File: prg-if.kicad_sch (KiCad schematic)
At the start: 30 parts

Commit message: Add power supply.
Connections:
- net P_5V_USB renamed PRG_USB_5V
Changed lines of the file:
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@@
     (effects (font (size 1.27 1.27)) (justify left))
   )
-  (hierarchical_label "P_5V_USB" (shape output) (at 46.99 92.71 0)
+  (hierarchical_label "PRG_USB_5V" (shape output) (at 46.99 92.71 0)
     (effects (font (size 1.27 1.27)) (justify left))
   )
@@
   )
   (symbol (lib_id "Interface_USB:FT2232HL") (at 129.54 114.3 0) (unit 1)
-    (in_bom yes) (on_board yes) (fields_autoplaced)
-    (property "Reference" "U?" (id 0) (at 144.2594 58.5302 0)
-      (effects (font (size 1.27 1.27)) (justify left))
-    )
-    (property "Value" "FT2232HL" (id 1) (at 144.2594 61.0671 0)
-      (effects (font (size 1.27 1.27)) (justify left))
-    )
+    (in_bom yes) (on_board yes)
+    (property "Reference" "U?" (id 0) (at 129.54 113.0331 0))
+    (property "Value" "FT2232HL" (id 1) (at 129.54 115.57 0))
     (property "Footprint" "Package_QFP:LQFP-64_10x10mm_P0.5mm" (id 2) (at 129.54 114.3 0)
       (effects (font (size 1.27 1.27)) hide)

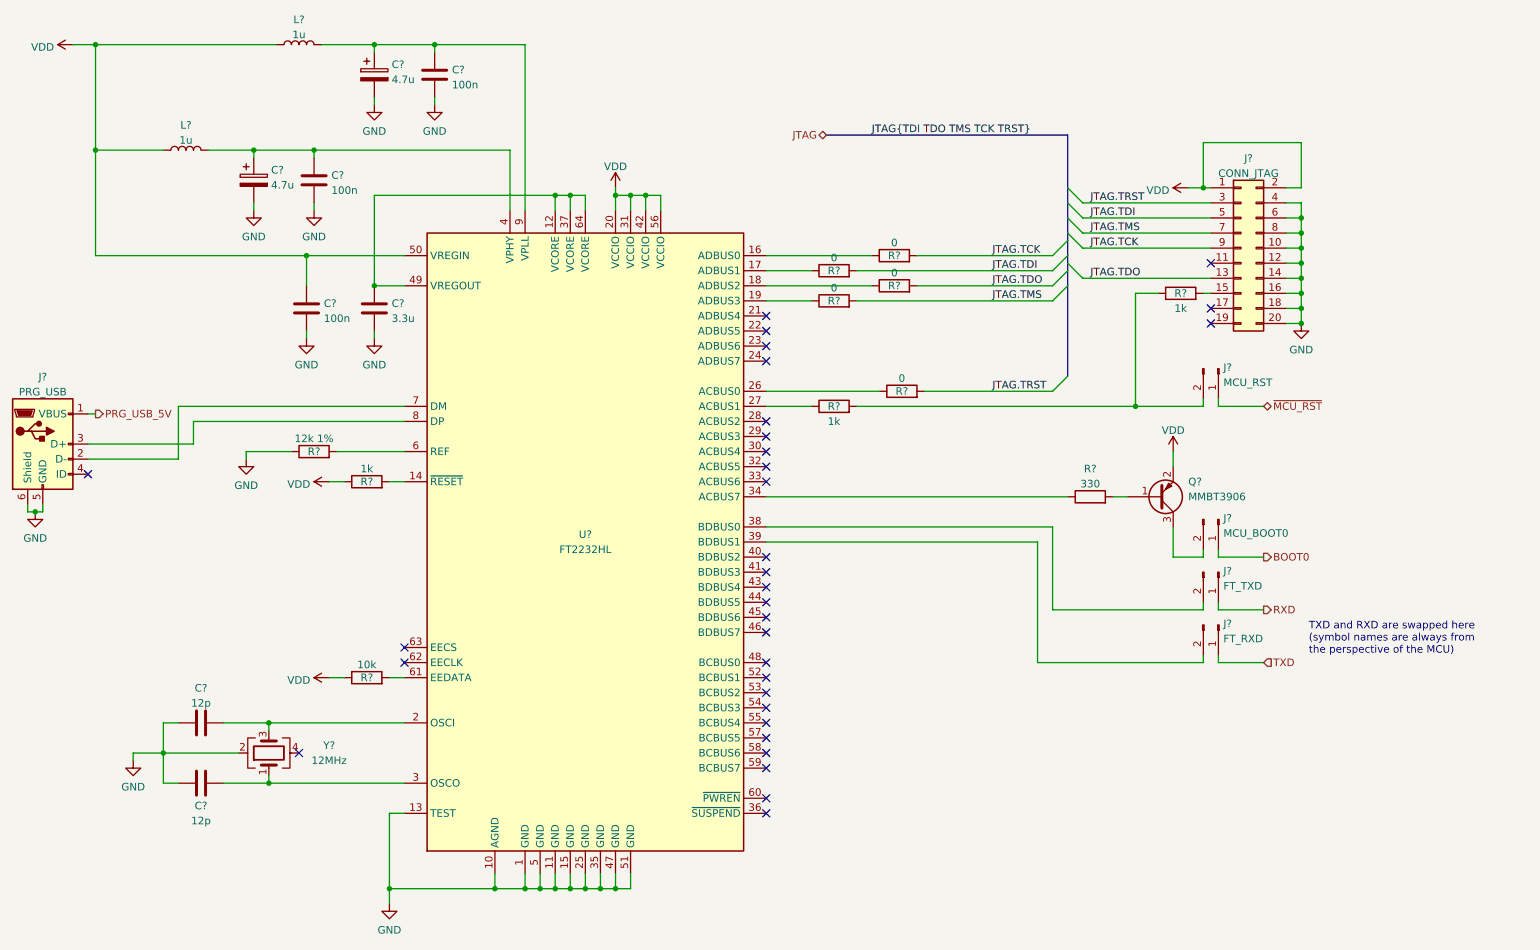
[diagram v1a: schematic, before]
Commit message: Capacitor part assignment
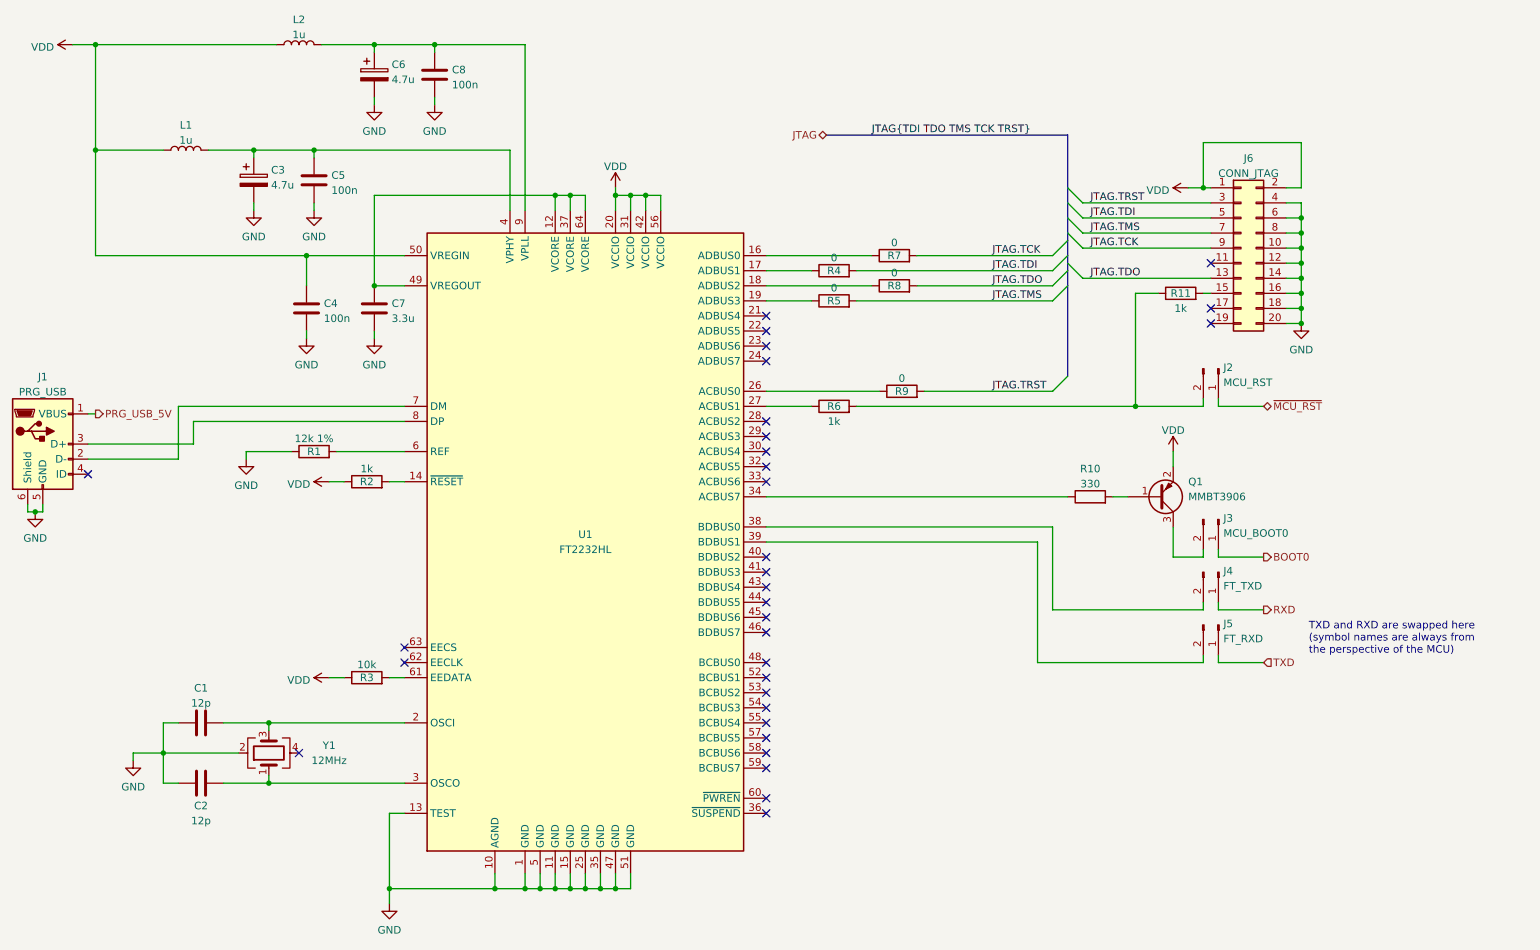
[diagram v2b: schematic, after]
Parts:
- C1, C2, C4, C5, C8: renamed from C?; footprint (none) -> Capacitor_SMD:C_0603_1608Metric_Pad1.08x0.95mm_HandSolder
- C3, C6: renamed from C?; footprint (none) -> Capacitor_Tantalum_SMD:CP_EIA-2012-15_AVX-P_Pad1.30x1.05mm_HandSolder; Part (none) -> 647-F920J475MPA
- C7: renamed from C?; footprint (none) -> Capacitor_SMD:C_0805_2012Metric_Pad1.18x1.45mm_HandSolder; Part (none) -> 963-LMK212B7335KG-T
- gave numbers to parts that had none: 22

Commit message: Final annotate pass
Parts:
- renumbered C1 to C201, C2 to C202, C3 to C203, C4 to C204, C5 to C205, C6 to C206, C7 to C207, C8 to C208, J1 to J201, J2 to J202, J3 to J203, J4 to J204, J5 to J205, J6 to J206, L1 to L201, L2 to L202, Q1 to Q201, R1 to R201, R2 to R202, R3 to R203, R4 to R204, R5 to R205, R6 to R206, R7 to R207, R8 to R208, R9 to R209, R10 to R210, R11 to R211, U1 to U201, Y1 to Y201

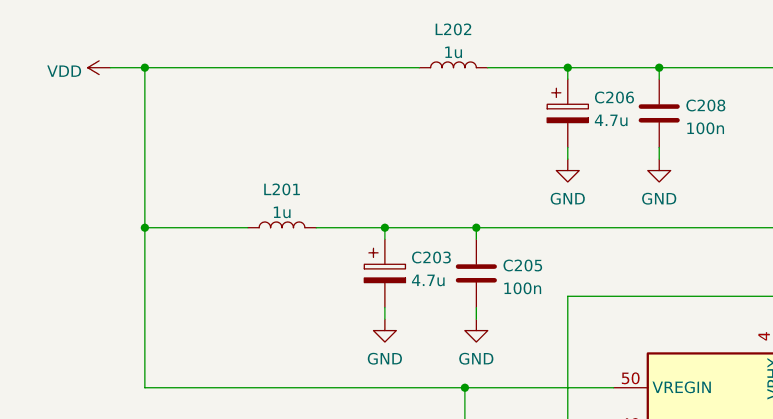
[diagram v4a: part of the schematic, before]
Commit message: Re-annotation, footprints
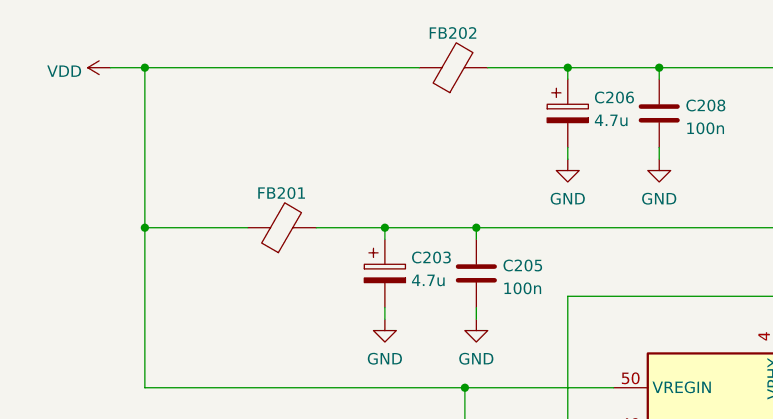
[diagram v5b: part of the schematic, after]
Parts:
- removed L201, L202: 1u, symbol Device:L
- added FB201, FB202: FerriteBead, Inductor_SMD:L_0603_1608Metric_Pad1.05x0.95mm_HandSolder, symbol Device:FerriteBead
- J201: footprint (none) -> Connector_USB:USB_Mini-B_Wuerth_65100516121_Horizontal
- J202, J203, J204, J205: footprint (none) -> Connector_PinHeader_2.54mm:PinHeader_1x02_P2.54mm_Vertical
- R201, R202, R203, R204, R205, R206, R207, R208, R209, R210, R211: footprint (none) -> Resistor_SMD:R_0603_1608Metric_Pad0.98x0.95mm_HandSolder
- Y201: footprint (none) -> Crystal:Crystal_SMD_5032-2Pin_5.0x3.2mm_HandSoldering
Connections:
- net VDD: now also FB201.1, FB202.1
- net at C203.1, C205.1, U201.4 (VPHY): now also FB201.2
- net at C206.1, C208.1, U201.9 (VPLL): now also FB202.2
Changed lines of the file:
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@@
     (pin "1")
-  )
-  (symbol (lib_id "Device:L") (at 62.23 48.26 90) (unit 1)
-    (in_bom yes) (on_board yes) (fields_autoplaced)
-    (property "Reference" "L201" (id 0) (at 62.23 44.0522 90))
-    (property "Value" "1u" (id 1) (at 62.23 46.5891 90))
-    (property "Footprint" "" (id 2) (at 62.23 48.26 0)
-      (effects (font (size 1.27 1.27)) hide)
-    )
-    (property "Datasheet" "~" (id 3) (at 62.23 48.26 0)
-      (effects (font (size 1.27 1.27)) hide)
-    )
-    (pin "1")
-    (pin "2")
   )
   (symbol (lib_id "Device:C") (at 93.98 74.93 0) (unit 1)
@@
     (property "Reference" "J201" (id 0) (at 38.1 86.4702 0))
     (property "Value" "PRG_USB" (id 1) (at 38.1 89.0071 0))
-    (property "Footprint" "" (id 2) (at 41.91 99.06 0)
+    (property "Footprint" "Connector_USB:USB_Mini-B_Wuerth_65100516121_Horizontal" (id 2) (at 41.91 99.06 0)
       (effects (font (size 1.27 1.27)) hide)
     )
@@
     (property "Reference" "R201" (id 0) (at 83.82 99.06 90))
     (property "Value" "12k 1%" (id 1) (at 83.82 96.8811 90))
-    (property "Footprint" "" (id 2) (at 83.82 100.838 90)
+    (property "Footprint" "Resistor_SMD:R_0603_1608Metric_Pad0.98x0.95mm_HandSolder" (id 2) (at 83.82 100.838 90)
       (effects (font (size 1.27 1.27)) hide)
     )
@@
     (property "Reference" "R204" (id 0) (at 171.45 68.58 90))
     (property "Value" "0" (id 1) (at 171.45 66.4011 90))
-    (property "Footprint" "" (id 2) (at 171.45 70.358 90)
+    (property "Footprint" "Resistor_SMD:R_0603_1608Metric_Pad0.98x0.95mm_HandSolder" (id 2) (at 171.45 70.358 90)
       (effects (font (size 1.27 1.27)) hide)
     )
@@
       (effects (font (size 1.27 1.27)) (justify left))
     )
-    (property "Footprint" "" (id 2) (at 236.22 119.38 0)
+    (property "Footprint" "Connector_PinHeader_2.54mm:PinHeader_1x02_P2.54mm_Vertical" (id 2) (at 236.22 119.38 0)
       (effects (font (size 1.27 1.27)) hide)
     )
@@
     (property "Reference" "R202" (id 0) (at 92.71 104.14 90))
     (property "Value" "1k" (id 1) (at 92.71 101.9611 90))
-    (property "Footprint" "" (id 2) (at 92.71 105.918 90)
+    (property "Footprint" "Resistor_SMD:R_0603_1608Metric_Pad0.98x0.95mm_HandSolder" (id 2) (at 92.71 105.918 90)
       (effects (font (size 1.27 1.27)) hide)
     )
@@
     (pin "3")
   )
-  (symbol (lib_id "Device:L") (at 81.28 30.48 90) (unit 1)
-    (in_bom yes) (on_board yes) (fields_autoplaced)
-    (property "Reference" "L202" (id 0) (at 81.28 26.2722 90))
-    (property "Value" "1u" (id 1) (at 81.28 28.8091 90))
-    (property "Footprint" "" (id 2) (at 81.28 30.48 0)
-      (effects (font (size 1.27 1.27)) hide)
-    )
-    (property "Datasheet" "~" (id 3) (at 81.28 30.48 0)
-      (effects (font (size 1.27 1.27)) hide)
-    )
-    (pin "1")
-    (pin "2")
-  )
   (symbol (lib_id "Device:R") (at 214.63 106.68 90) (unit 1)
     (in_bom yes) (on_board yes) (fields_autoplaced)
     (property "Reference" "R210" (id 0) (at 214.63 101.9642 90))
     (property "Value" "330" (id 1) (at 214.63 104.5011 90))
-    (property "Footprint" "" (id 2) (at 214.63 108.458 90)
+    (property "Footprint" "Resistor_SMD:R_0603_1608Metric_Pad0.98x0.95mm_HandSolder" (id 2) (at 214.63 108.458 90)
       (effects (font (size 1.27 1.27)) hide)
     )
@@
     (property "Reference" "R207" (id 0) (at 181.61 66.04 90))
     (property "Value" "0" (id 1) (at 181.61 63.8611 90))
-    (property "Footprint" "" (id 2) (at 181.61 67.818 90)
+    (property "Footprint" "Resistor_SMD:R_0603_1608Metric_Pad0.98x0.95mm_HandSolder" (id 2) (at 181.61 67.818 90)
       (effects (font (size 1.27 1.27)) hide)
     )
     (property "Datasheet" "~" (id 3) (at 181.61 66.04 0)
+      (effects (font (size 1.27 1.27)) hide)
+    )
+    (pin "1")
+    (pin "2")
+  )
+  (symbol (lib_id "Device:FerriteBead") (at 62.23 48.26 90) (unit 1)
+    (in_bom yes) (on_board yes) (fields_autoplaced)
+    (property "Reference" "FB201" (id 0) (at 62.1792 44.4556 90))
+    (property "Value" "FerriteBead" (id 1) (at 62.1792 44.4555 90)
+      (effects (font (size 1.27 1.27)) hide)
+    )
+    (property "Footprint" "Inductor_SMD:L_0603_1608Metric_Pad1.05x0.95mm_HandSolder" (id 2) (at 62.23 50.038 90)
+      (effects (font (size 1.27 1.27)) hide)
+    )
+    (property "Datasheet" "~" (id 3) (at 62.23 48.26 0)
+      (effects (font (size 1.27 1.27)) hide)
+    )
+    (property "Part" "815-ACML-0603H-301" (id 4) (at 62.23 48.26 90)
       (effects (font (size 1.27 1.27)) hide)
     )
@@
     (property "Reference" "R208" (id 0) (at 181.61 71.12 90))
     (property "Value" "0" (id 1) (at 181.61 68.9411 90))
-    (property "Footprint" "" (id 2) (at 181.61 72.898 90)
+    (property "Footprint" "Resistor_SMD:R_0603_1608Metric_Pad0.98x0.95mm_HandSolder" (id 2) (at 181.61 72.898 90)
       (effects (font (size 1.27 1.27)) hide)
     )
@@
     (property "Reference" "R206" (id 0) (at 171.45 91.44 90))
     (property "Value" "1k" (id 1) (at 171.45 93.98 90))
-    (property "Footprint" "" (id 2) (at 171.45 93.218 90)
+    (property "Footprint" "Resistor_SMD:R_0603_1608Metric_Pad0.98x0.95mm_HandSolder" (id 2) (at 171.45 93.218 90)
       (effects (font (size 1.27 1.27)) hide)
     )
@@
     (pin "2")
   )
+  (symbol (lib_id "Device:FerriteBead") (at 81.28 30.48 90) (unit 1)
+    (in_bom yes) (on_board yes) (fields_autoplaced)
+    (property "Reference" "FB202" (id 0) (at 81.2292 26.6756 90))
+    (property "Value" "FerriteBead" (id 1) (at 81.2292 26.6755 90)
+      (effects (font (size 1.27 1.27)) hide)
+    )
+    (property "Footprint" "Inductor_SMD:L_0603_1608Metric_Pad1.05x0.95mm_HandSolder" (id 2) (at 81.28 32.258 90)
+      (effects (font (size 1.27 1.27)) hide)
+    )
+    (property "Datasheet" "~" (id 3) (at 81.28 30.48 0)
+      (effects (font (size 1.27 1.27)) hide)
+    )
+    (property "Part" "815-ACML-0603H-301" (id 4) (at 81.28 30.48 90)
+      (effects (font (size 1.27 1.27)) hide)
+    )
+    (pin "1")
+    (pin "2")
+  )
   (symbol (lib_id "Connector:Conn_01x02_Male") (at 236.22 128.27 270) (unit 1)
     (in_bom yes) (on_board yes) (fields_autoplaced)
@@
       (effects (font (size 1.27 1.27)) (justify left))
     )
-    (property "Footprint" "" (id 2) (at 236.22 128.27 0)
+    (property "Footprint" "Connector_PinHeader_2.54mm:PinHeader_1x02_P2.54mm_Vertical" (id 2) (at 236.22 128.27 0)
       (effects (font (size 1.27 1.27)) hide)
     )
@@
     (property "Reference" "R211" (id 0) (at 229.87 72.39 90))
     (property "Value" "1k" (id 1) (at 229.87 74.93 90))
-    (property "Footprint" "" (id 2) (at 229.87 74.168 90)
+    (property "Footprint" "Resistor_SMD:R_0603_1608Metric_Pad0.98x0.95mm_HandSolder" (id 2) (at 229.87 74.168 90)
       (effects (font (size 1.27 1.27)) hide)
     )
@@
     (property "Reference" "R209" (id 0) (at 182.88 88.9 90))
     (property "Value" "0" (id 1) (at 182.88 86.7211 90))
-    (property "Footprint" "" (id 2) (at 182.88 90.678 90)
+    (property "Footprint" "Resistor_SMD:R_0603_1608Metric_Pad0.98x0.95mm_HandSolder" (id 2) (at 182.88 90.678 90)
       (effects (font (size 1.27 1.27)) hide)
     )
@@
     (property "Reference" "R203" (id 0) (at 92.71 137.16 90))
     (property "Value" "10k" (id 1) (at 92.71 134.9811 90))
-    (property "Footprint" "" (id 2) (at 92.71 138.938 90)
+    (property "Footprint" "Resistor_SMD:R_0603_1608Metric_Pad0.98x0.95mm_HandSolder" (id 2) (at 92.71 138.938 90)
       (effects (font (size 1.27 1.27)) hide)
     )
@@
     (property "Reference" "R205" (id 0) (at 171.45 73.66 90))
     (property "Value" "0" (id 1) (at 171.45 71.4811 90))
-    (property "Footprint" "" (id 2) (at 171.45 75.438 90)
+    (property "Footprint" "Resistor_SMD:R_0603_1608Metric_Pad0.98x0.95mm_HandSolder" (id 2) (at 171.45 75.438 90)
       (effects (font (size 1.27 1.27)) hide)
     )
@@
     (property "Reference" "Y201" (id 0) (at 86.36 148.5931 90))
     (property "Value" "12MHz" (id 1) (at 86.36 151.13 90))
-    (property "Footprint" "" (id 2) (at 76.2 149.86 0)
+    (property "Footprint" "Crystal:Crystal_SMD_5032-2Pin_5.0x3.2mm_HandSoldering" (id 2) (at 76.2 149.86 0)
       (effects (font (size 1.27 1.27)) hide)
     )
@@
       (effects (font (size 1.27 1.27)) (justify left))
     )
-    (property "Footprint" "" (id 2) (at 236.22 110.49 0)
+    (property "Footprint" "Connector_PinHeader_2.54mm:PinHeader_1x02_P2.54mm_Vertical" (id 2) (at 236.22 110.49 0)
       (effects (font (size 1.27 1.27)) hide)
     )
@@
       (effects (font (size 1.27 1.27)) (justify left))
     )
-    (property "Footprint" "" (id 2) (at 236.22 85.09 0)
-      (effects (font (size 1.27 1.27)) hide)
-    )
+    (property "Footprint" "Connector_PinHeader_2.54mm:PinHeader_1x02_P2.54mm_Vertical" (id 2) (at 236.22 85.09 0)
+      (effects (font (size 1.27 1.27)) hide)
+    )

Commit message: More footprints
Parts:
- J206: footprint (none) -> Connector_PinSocket_2.54mm:PinSocket_2x10_P2.54mm_Vertical
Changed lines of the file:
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@@
     (property "Reference" "J206" (id 0) (at 241.3 49.6402 0))
     (property "Value" "CONN_JTAG" (id 1) (at 241.3 52.1771 0))
-    (property "Footprint" "" (id 2) (at 240.03 64.77 0)
+    (property "Footprint" "Connector_PinSocket_2.54mm:PinSocket_2x10_P2.54mm_Vertical" (id 2) (at 240.03 64.77 0)
       (effects (font (size 1.27 1.27)) hide)
     )

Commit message: Placement almost complete
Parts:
- Y201: footprint Crystal:Crystal_SMD_5032-2Pin_5.0x3.2mm_HandSoldering -> Crystal:Crystal_SMD_5032-4Pin_5.0x3.2mm
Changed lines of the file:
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@@
     (property "Reference" "Y201" (id 0) (at 86.36 148.5931 90))
     (property "Value" "12MHz" (id 1) (at 86.36 151.13 90))
-    (property "Footprint" "Crystal:Crystal_SMD_5032-2Pin_5.0x3.2mm_HandSoldering" (id 2) (at 76.2 149.86 0)
+    (property "Footprint" "Crystal:Crystal_SMD_5032-4Pin_5.0x3.2mm" (id 2) (at 76.2 149.86 0)
       (effects (font (size 1.27 1.27)) hide)
     )

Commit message: Add worksheet template with PoliMi logo.
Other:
- title: (none) -> MARCO RAM Board
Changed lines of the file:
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@@
 (kicad_sch (version 20211123) (generator eeschema)
   (paper "A4")
+  (title_block
+    (title "MARCO RAM Board")
+    (rev "1")
+    (comment 9 "Programming Interface")
+  )
   (junction (at 250.19 59.69) (diameter 0) (color 0 0 0 0)
   )
